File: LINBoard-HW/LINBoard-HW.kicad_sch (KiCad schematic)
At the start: 0 parts

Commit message: board layout started
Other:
- sheet Connectors ports: added none; removed ENABLE
- sheet Microcontroller ports: added none; removed ENABLE
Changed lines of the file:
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@@
-	(wire
-		(pts
-			(xy 170.18 55.88) (xy 179.07 55.88)
-		)
-		(stroke
-			(width 0)
-			(type default)
-		)
-	)
 	(wire
 		(pts
@@
 	(global_label "CAN_L"
 		(shape bidirectional)
-		(at 204.47 74.93 0)
+		(at 204.47 97.79 0)
 		(fields_autoplaced yes)
 		(effects
@@
 		)
 		(property "Intersheetrefs" "${INTERSHEET_REFS}"
-			(at 214.2513 74.93 0)
+			(at 214.2513 97.79 0)
 			(effects
 				(font
@@
 	(global_label "CAN_H"
 		(shape bidirectional)
-		(at 204.47 71.12 0)
+		(at 204.47 93.98 0)
 		(fields_autoplaced yes)
 		(effects
@@
 		)
 		(property "Intersheetrefs" "${INTERSHEET_REFS}"
-			(at 214.5537 71.12 0)
+			(at 214.5537 93.98 0)
 			(effects
 				(font
@@
 	(global_label "LIN"
 		(shape bidirectional)
-		(at 204.47 59.69 0)
+		(at 204.47 90.17 0)
 		(fields_autoplaced yes)
 		(effects
@@
 		)
 		(property "Intersheetrefs" "${INTERSHEET_REFS}"
-			(at 211.5299 59.69 0)
+			(at 211.5299 90.17 0)
 			(effects
 				(font
@@
 	)
 	(sheet
-		(at 179.07 52.832)
-		(size 25.4 51.816)
+		(at 179.07 86.36)
+		(size 25.4 18.288)
 		(exclude_from_sim no)
 		(in_bom yes)
@@
 		)
 		(property "Sheetname" "Connectors"
-			(at 179.07 52.1204 0)
+			(at 179.07 85.6484 0)
 			(effects
 				(font
@@
 		)
 		(pin "LIN" bidirectional
-			(at 204.47 59.69 0)
+			(at 204.47 90.17 0)
 			(effects
 				(font
@@
 		)
 		(pin "CAN_H" bidirectional
-			(at 204.47 71.12 0)
+			(at 204.47 93.98 0)
 			(effects
 				(font
@@
 		)
 		(pin "CAN_L" bidirectional
-			(at 204.47 74.93 0)
+			(at 204.47 97.79 0)
 			(effects
 				(font
@@
 		(pin "USB_D-" bidirectional
 			(at 179.07 97.79 180)
-			(effects
-				(font
-					(size 1.27 1.27)
-				)
-				(justify left)
-			)
-		)
-		(pin "ENABLE" output
-			(at 179.07 55.88 180)
 			(effects
 				(font
@@
 			)
 		)
-		(pin "ENABLE" input
-			(at 170.18 55.88 0)
-			(effects
-				(font
-					(size 1.27 1.27)
-				)
-				(justify right)
-			)
-		)

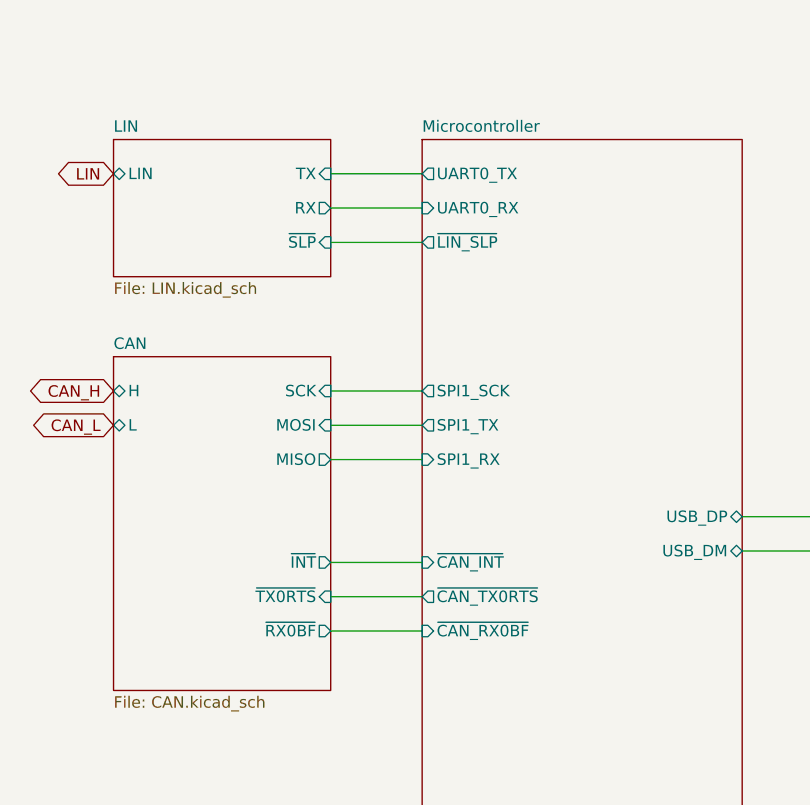
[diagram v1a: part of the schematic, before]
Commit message: change usb
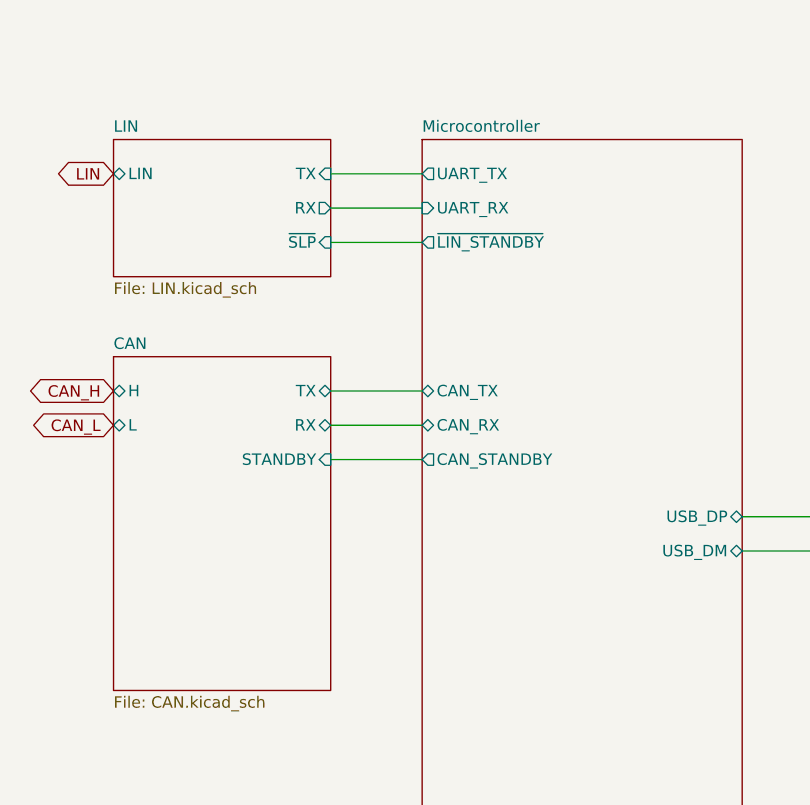
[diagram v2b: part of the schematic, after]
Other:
- sheet CAN ports: added RX, STANDBY, TX; removed MISO, MOSI, SCK, ~{INT}, ~{RX0BF}, ~{TX0RTS}
- sheet Microcontroller ports: added CAN_RX, CAN_STANDBY, CAN_TX, UART_RX, UART_TX, ~{LIN_STANDBY}; removed SPI1_RX, SPI1_SCK, SPI1_TX, UART0_RX, UART0_TX, ~{CAN_INT}, ~{CAN_RX0BF}, ~{CAN_TX0RTS}, ~{LIN_SLP}
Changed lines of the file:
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@@
 	(title_block
 		(title "LINBoard")
-		(date "2025-07-11")
+		(date "2025-08-11")
 		(rev "V1")
 		(company "Dingo Electronics")
@@
 	(wire
 		(pts
+			(xy 124.46 83.82) (xy 134.62 83.82)
+		)
+		(stroke
+			(width 0)
+			(type default)
+		)
+	)
+	(wire
+		(pts
+			(xy 124.46 63.5) (xy 134.62 63.5)
+		)
+		(stroke
+			(width 0)
+			(type default)
+		)
+	)
+	(wire
+		(pts
+			(xy 124.46 87.63) (xy 134.62 87.63)
+		)
+		(stroke
+			(width 0)
+			(type default)
+		)
+	)
+	(wire
+		(pts
+			(xy 170.18 93.98) (xy 179.07 93.98)
+		)
+		(stroke
+			(width 0)
+			(type default)
+		)
+	)
+	(wire
+		(pts
+			(xy 170.18 97.79) (xy 179.07 97.79)
+		)
+		(stroke
+			(width 0)
+			(type default)
+		)
+	)
+	(wire
+		(pts
+			(xy 124.46 80.01) (xy 134.62 80.01)
+		)
+		(stroke
+			(width 0)
+			(type default)
+		)
+	)
+	(wire
+		(pts
 			(xy 124.46 59.69) (xy 134.62 59.69)
 		)
@@
 	(wire
 		(pts
-			(xy 124.46 102.87) (xy 134.62 102.87)
-		)
-		(stroke
-			(width 0)
-			(type default)
-		)
-	)
-	(wire
-		(pts
 			(xy 124.46 55.88) (xy 134.62 55.88)
-		)
-		(stroke
-			(width 0)
-			(type default)
-		)
-	)
-	(wire
-		(pts
-			(xy 124.46 63.5) (xy 134.62 63.5)
-		)
-		(stroke
-			(width 0)
-			(type default)
-		)
-	)
-	(wire
-		(pts
-			(xy 124.46 87.63) (xy 134.62 87.63)
-		)
-		(stroke
-			(width 0)
-			(type default)
-		)
-	)
-	(wire
-		(pts
-			(xy 170.18 93.98) (xy 179.07 93.98)
-		)
-		(stroke
-			(width 0)
-			(type default)
-		)
-	)
-	(wire
-		(pts
-			(xy 170.18 97.79) (xy 179.07 97.79)
-		)
-		(stroke
-			(width 0)
-			(type default)
-		)
-	)
-	(wire
-		(pts
-			(xy 124.46 83.82) (xy 134.62 83.82)
-		)
-		(stroke
-			(width 0)
-			(type default)
-		)
-	)
-	(wire
-		(pts
-			(xy 124.46 80.01) (xy 134.62 80.01)
-		)
-		(stroke
-			(width 0)
-			(type default)
-		)
-	)
-	(wire
-		(pts
-			(xy 124.46 106.68) (xy 134.62 106.68)
-		)
-		(stroke
-			(width 0)
-			(type default)
-		)
-	)
-	(wire
-		(pts
-			(xy 124.46 99.06) (xy 134.62 99.06)
 		)
 		(stroke
@@
 			)
 		)
-		(pin "~{TX0RTS}" input
-			(at 124.46 102.87 0)
-			(effects
-				(font
-					(size 1.27 1.27)
-				)
-				(justify right)
-			)
-		)
-		(pin "MOSI" input
+		(pin "TX" bidirectional
+			(at 124.46 80.01 0)
+			(effects
+				(font
+					(size 1.27 1.27)
+				)
+				(justify right)
+			)
+		)
+		(pin "RX" bidirectional
 			(at 124.46 83.82 0)
 			(effects
@@
 			)
 		)
-		(pin "SCK" input
-			(at 124.46 80.01 0)
-			(effects
-				(font
-					(size 1.27 1.27)
-				)
-				(justify right)
-			)
-		)
-		(pin "~{RX0BF}" output
-			(at 124.46 106.68 0)
-			(effects
-				(font
-					(size 1.27 1.27)
-				)
-				(justify right)
-			)
-		)
-		(pin "~{INT}" output
-			(at 124.46 99.06 0)
-			(effects
-				(font
-					(size 1.27 1.27)
-				)
-				(justify right)
-			)
-		)
-		(pin "MISO" output
+		(pin "STANDBY" input
 			(at 124.46 87.63 0)
 			(effects
@@
 			)
 		)
-		(pin "~{CAN_INT}" input
-			(at 134.62 99.06 180)
-			(effects
-				(font
-					(size 1.27 1.27)
-				)
-				(justify left)
-			)
-		)
-		(pin "~{CAN_RX0BF}" input
-			(at 134.62 106.68 180)
-			(effects
-				(font
-					(size 1.27 1.27)
-				)
-				(justify left)
-			)
-		)
-		(pin "~{CAN_TX0RTS}" output
-			(at 134.62 102.87 180)
-			(effects
-				(font
-					(size 1.27 1.27)
-				)
-				(justify left)
-			)
-		)
-		(pin "~{LIN_SLP}" output
+		(pin "CAN_RX" bidirectional
+			(at 134.62 83.82 180)
+			(effects
+				(font
+					(size 1.27 1.27)
+				)
+				(justify left)
+			)
+		)
+		(pin "CAN_TX" bidirectional
+			(at 134.62 80.01 180)
+			(effects
+				(font
+					(size 1.27 1.27)
+				)
+				(justify left)
+			)
+		)
+		(pin "CAN_STANDBY" output
+			(at 134.62 87.63 180)
+			(effects
+				(font
+					(size 1.27 1.27)
+				)
+				(justify left)
+			)
+		)
+		(pin "~{LIN_STANDBY}" output
 			(at 134.62 63.5 180)
 			(effects
@@
 			)
 		)
-		(pin "SPI1_RX" input
-			(at 134.62 87.63 180)
-			(effects
-				(font
-					(size 1.27 1.27)
-				)
-				(justify left)
-			)
-		)
-		(pin "SPI1_SCK" output
-			(at 134.62 80.01 180)
-			(effects
-				(font
-					(size 1.27 1.27)
-				)
-				(justify left)
-			)
-		)
-		(pin "SPI1_TX" output
-			(at 134.62 83.82 180)
-			(effects
-				(font
-					(size 1.27 1.27)
-				)
-				(justify left)
-			)
-		)
-		(pin "UART0_RX" input
+		(pin "UART_RX" input
 			(at 134.62 59.69 180)
 			(effects
@@
 			)
 		)
-		(pin "UART0_TX" output
+		(pin "UART_TX" output
 			(at 134.62 55.88 180)
 			(effects

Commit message: doing some layout
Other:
- sheet Microcontroller ports: added UART2_RX, UART2_TX; removed UART_RX, UART_TX
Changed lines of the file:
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@@
 			)
 		)
-		(pin "UART_RX" input
+		(pin "UART2_RX" input
 			(at 134.62 59.69 180)
 			(effects
@@
 			)
 		)
-		(pin "UART_TX" output
+		(pin "UART2_TX" output
 			(at 134.62 55.88 180)
 			(effects

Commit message: fixed some trace widths
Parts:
- added G1: DingoFace, DRTLogo:DingoFaceNoFill, symbol DRT_Logo:DRT_Logo
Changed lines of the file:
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@@
+		)
+	)
+	(symbol
+		(lib_id "DRT_Logo:DRT_Logo")
+		(at 271.78 161.29 0)
+		(unit 1)
+		(exclude_from_sim no)
+		(in_bom yes)
+		(on_board yes)
+		(dnp no)
+		(fields_autoplaced yes)
+		(property "Reference" "G1"
+			(at 273.05 160.0199 0)
+			(effects
+				(font
+					(size 1.27 1.27)
+				)
+				(justify left)
+			)
+		)
+		(property "Value" "DingoFace"
+			(at 273.05 162.5599 0)
+			(effects
+				(font
+					(size 1.27 1.27)
+				)
+				(justify left)
+			)
+		)
+		(property "Footprint" "DRTLogo:DingoFaceNoFill"
+			(at 271.78 161.29 0)
+			(effects
+				(font
+					(size 1.27 1.27)
+				)
+				(hide yes)
+			)
+		)
+		(property "Datasheet" ""
+			(at 271.78 161.29 0)
+			(effects
+				(font
+					(size 1.27 1.27)
+				)
+				(hide yes)
+			)
+		)
+		(property "Description" ""
+			(at 271.78 161.29 0)
+			(effects
+				(font
+					(size 1.27 1.27)
+				)
+				(hide yes)
+			)
+		)
+		(instances
+			(project ""
+				(path "/27863e5d-8a22-474c-850d-36d8970b0f4a"
+					(reference "G1")
+					(unit 1)
+				)
+			)
 		)
 	)

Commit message: add fab outputs
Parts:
- G1: now left out of the parts list
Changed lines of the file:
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@@
 		(unit 1)
 		(exclude_from_sim no)
-		(in_bom yes)
+		(in_bom no)
 		(on_board yes)
 		(dnp no)
@@
 			(at 271.78 161.29 0)
 			(effects
+				(font
+					(size 1.27 1.27)
+				)
+				(hide yes)
+			)
+		)
+		(property "LCSC Part" ""
+			(at 271.78 161.29 0)
+			(effects

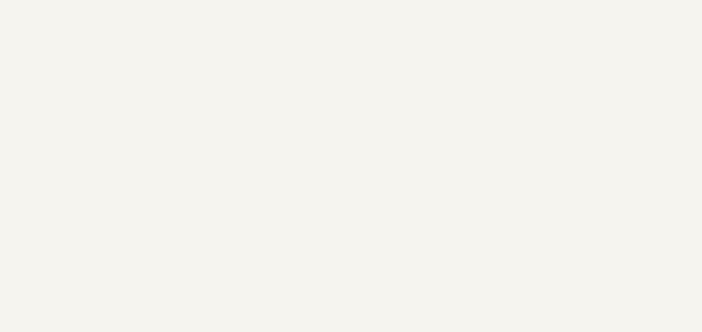
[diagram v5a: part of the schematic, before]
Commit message: add tvs, fix reset button
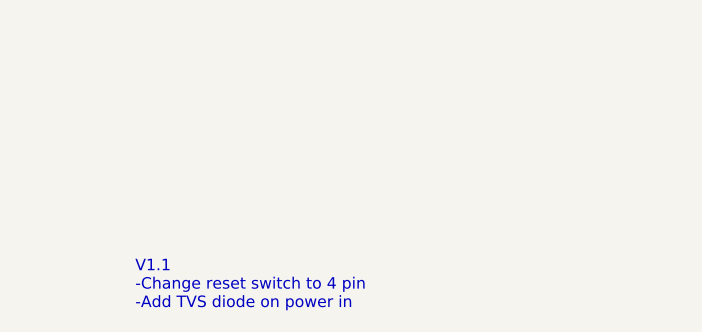
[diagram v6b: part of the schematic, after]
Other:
- note added: "V1.1 -Change reset switch to 4 pin -Add TVS diode on power in"
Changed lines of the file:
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@@
 		(comment 1 "Cory Grant")
+	)
+	(text "V1.1\n-Change reset switch to 4 pin\n-Add TVS diode on power in"
+		(exclude_from_sim no)
+		(at 31.496 164.084 0)
+		(effects
+			(font
+				(size 1.27 1.27)
+			)
+			(justify left)
+		)
 	)
 	(wire
